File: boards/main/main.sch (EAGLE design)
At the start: 28 parts, among them IC1 LSM330DLC-LGA28, IC2 PIC16(L)F1454-TSSOP-14, IC3 TPS60502-DGS, J1 RJ11-6PTH, Q1 BC547B, Q2 BC547B

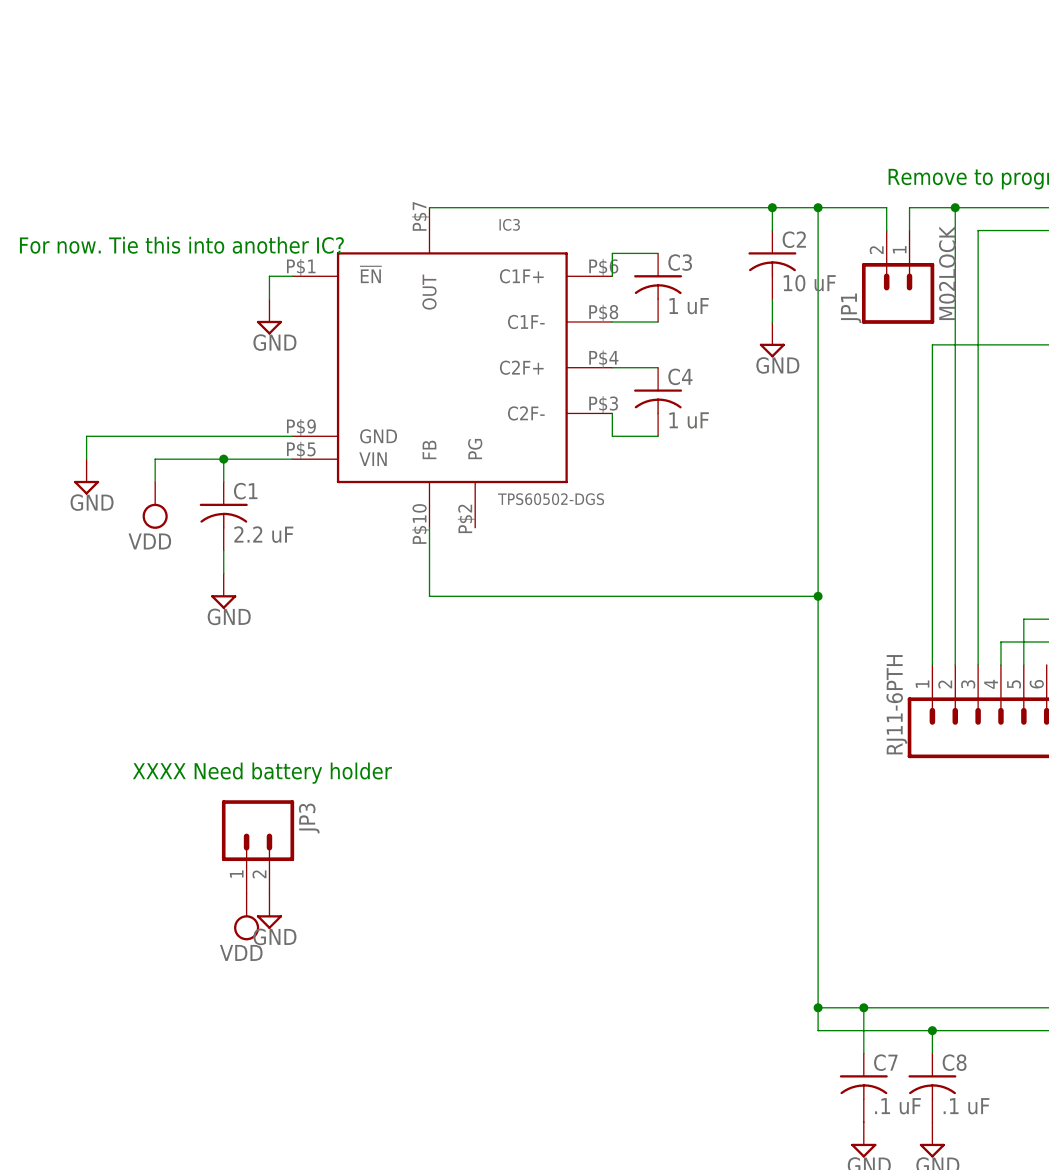
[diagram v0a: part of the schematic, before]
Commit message: Added Linear Technology micropower regulator (1.8V) part and schematic.
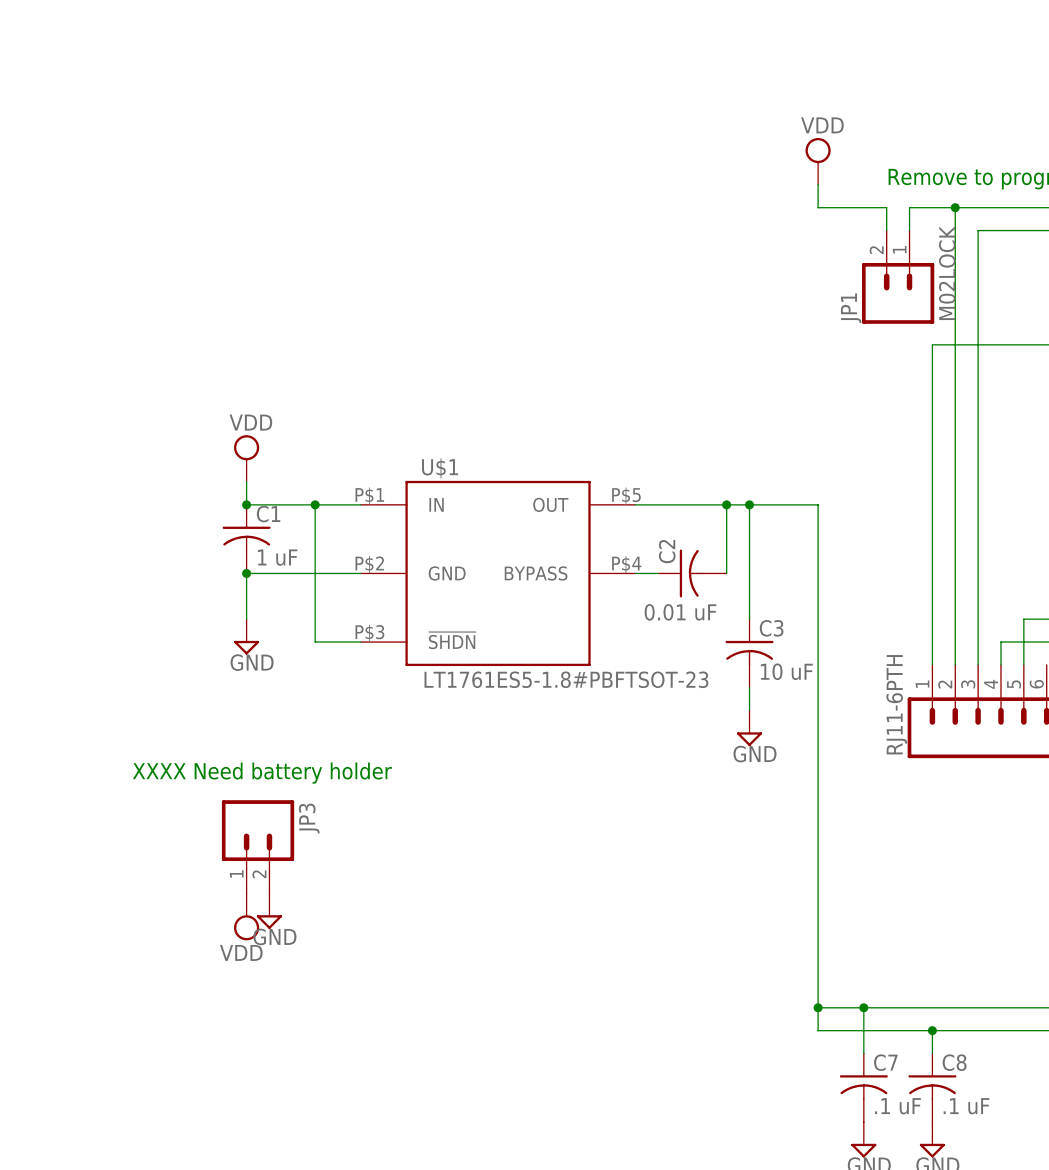
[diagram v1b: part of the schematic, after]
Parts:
- removed C4: 1 uF, rcl:C-USC0805
- removed IC3: TPS60502-DGS, leds:TPS60502-DGS
- added U$1: LT1761ES5-1.8#PBFTSOT-23, leds:LT1761ES5-1.8#PBFTSOT-23
- C1: value 2.2 uF -> 1 uF; device rcl:C-USC0805 -> rcl:C-USC1206
- C2: value 10 uF -> 0.01 uF
- C3: value 1 uF -> 10 uF; device rcl:C-USC0805 -> rcl:C-USC1206
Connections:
- removed net N$3: C3.2, IC3.C1F-
- removed net N$4: C4.1, IC3.C2F+
- removed net N$5: C4.2, IC3.C2F-
- net GND: now also C3.2, U$1.GND; no longer C2.2, IC3.!EN!, IC3.GND
- net N$1: now also C2.2, C3.1, U$1.OUT; no longer C2.1, IC3.FB, IC3.OUT, JP1.2
- net N$2: now also C2.1, U$1.BYPASS; no longer C3.1, IC3.C1F+
- net VDD: now also JP1.2, U$1.!SHDN!, U$1.IN; no longer IC3.VIN
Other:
- note removed: "For now. Tie this into another IC?"
- moved on the sheet: C1, C2, C3
